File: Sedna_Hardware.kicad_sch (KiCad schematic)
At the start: 50 parts, among them J1 PJ-102A, J10 2-644803-3, J11 2-644488-3, J2 1935161, J3 1935161, J4 2-644488-2, J5 61201021721, J6 5-103634-2, J7 0878340619, J8 Conn_01x14, J9 2-644803-3, K1 ALDP105W, K2 ALDP105W, Q1 2N7000-D75Z, Q2 2N7000-D75Z, U1 LD1117V33, U2 ESP32-WROOM-32D-N16, U3 LM6511IMX/NOPB

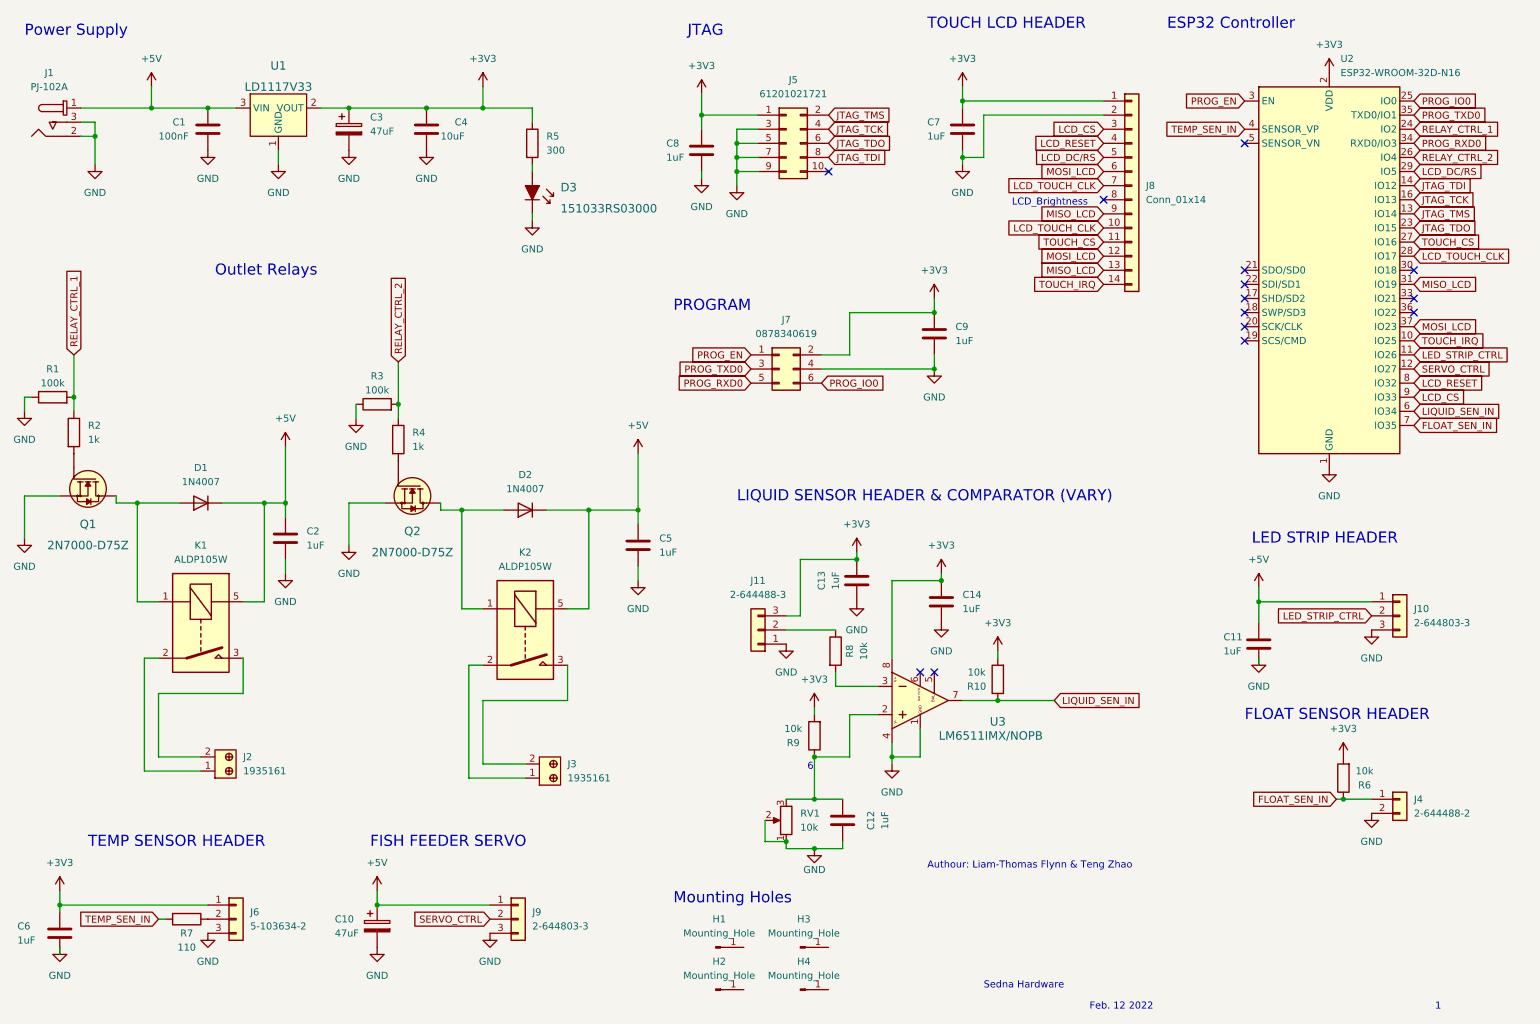
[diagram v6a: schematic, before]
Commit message: started layout tracks. Fixed regulator footprint
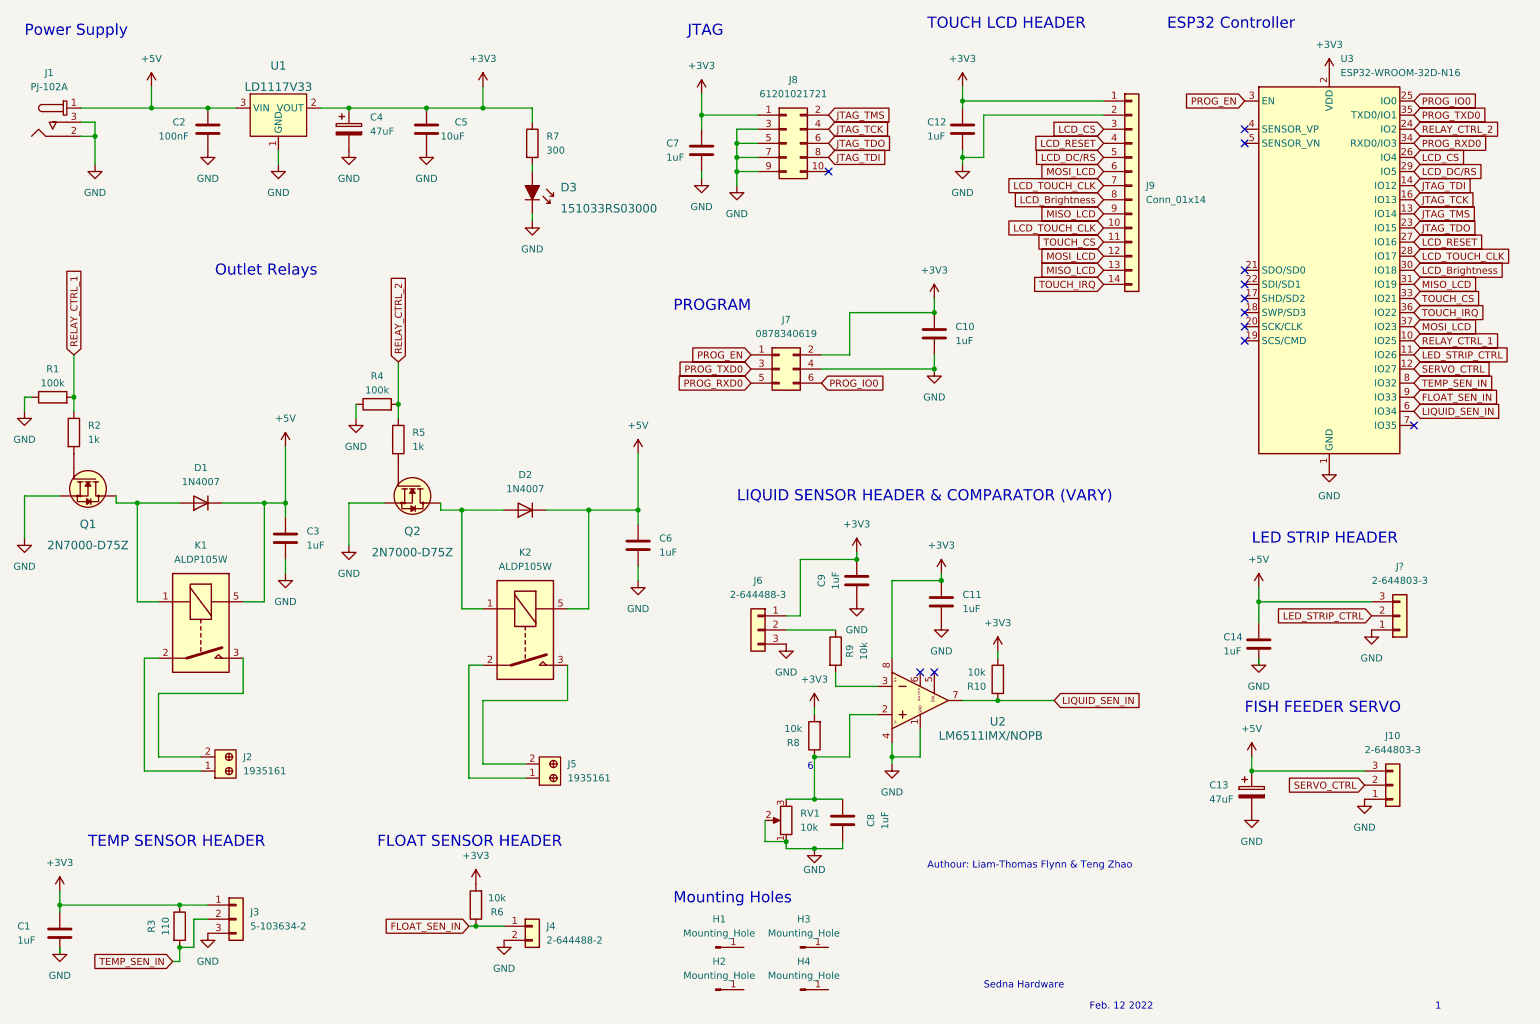
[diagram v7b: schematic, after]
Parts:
- removed J11: 2-644488-3, 2-644488-3:TE_2-644488-3, symbol Connector_Generic:Conn_01x03
- removed J9: 2-644803-3, 2-644803-3:TE_2-644803-3, symbol Connector_Generic:Conn_01x03
- removed R7: 110, Resistor_THT:R_Axial_DIN0204_L3.6mm_D1.6mm_P5.08mm_Horizontal, symbol Device:R
- added J6: 2-644488-3, 2-644488-3:TE_2-644488-3, symbol Connector_Generic:Conn_01x03
- added J?: 2-644803-3, 2-644803-3:TE_2-644803-3, symbol Connector_Generic:Conn_01x03
- added R3: 110, Resistor_THT:R_Axial_DIN0204_L3.6mm_D1.6mm_P5.08mm_Horizontal, symbol Device:R
- U1: footprint Package_TO_SOT_THT:TO-220-3_Horizontal_TabDown -> Package_TO_SOT_THT:TO-220-3_Horizontal_TabUp
- renumbered C6 to C1, C9 to C10, C14 to C11, C7 to C12, C10 to C13, C11 to C14, C1 to C2, C2 to C3, C3 to C4, C4 to C5, C5 to C6, C8 to C7, C12 to C8, C13 to C9, J6 to J3, J3 to J5, J5 to J8, J8 to J9, R3 to R4, R4 to R5, R5 to R7, R9 to R8, R8 to R9, U3 to U2, U2 to U3
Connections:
- net +3V3: now also J6.1 (Pin_1), R3.1
- net +5V: now also J10.3 (Pin_3), J?.3 (Pin_3); no longer J10.1 (Pin_1)
- net FLOAT_SEN_IN: now also U3.9 (IO33); no longer U3.7 (IO35)
- net GND: now also J10.1 (Pin_1), J6.3 (Pin_3), J?.1 (Pin_1); no longer J10.3 (Pin_3)
- net LCD_CS: now also U3.26 (IO4); no longer U3.9 (IO33)
- net LCD_RESET: now also U3.27 (IO16); no longer U3.8 (IO32)
- net LED_STRIP_CTRL: now also J?.2 (Pin_2); no longer J10.2 (Pin_2)
- net RELAY_CTRL_1: now also U3.10 (IO25); no longer U3.24 (IO2)
- net RELAY_CTRL_2: now also U3.24 (IO2); no longer U3.26 (IO4)
- net SERVO_CTRL: now also J10.2 (Pin_2)
- net TEMP_SEN_IN: now also J3.2 (Pin_2), U3.8 (IO32), R3.2; no longer U3.4 (SENSOR_VP)
- net TOUCH_CS: now also U3.33 (IO21); no longer U3.27 (IO16)
- net TOUCH_IRQ: now also U3.36 (IO22); no longer U3.10 (IO25)
- net LCD_Brightness: now reaches U3.30 (IO18)
- net LCD_Brightness: now also J9.8 (Pin_8)
- net at R9.1: now also J6.2 (Pin_2)
- no-connect marks 14 -> 12
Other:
- note removed: "LCD_Brightness"
- moved on the sheet: C13, J4, R6

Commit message: adjusted track size of power bus
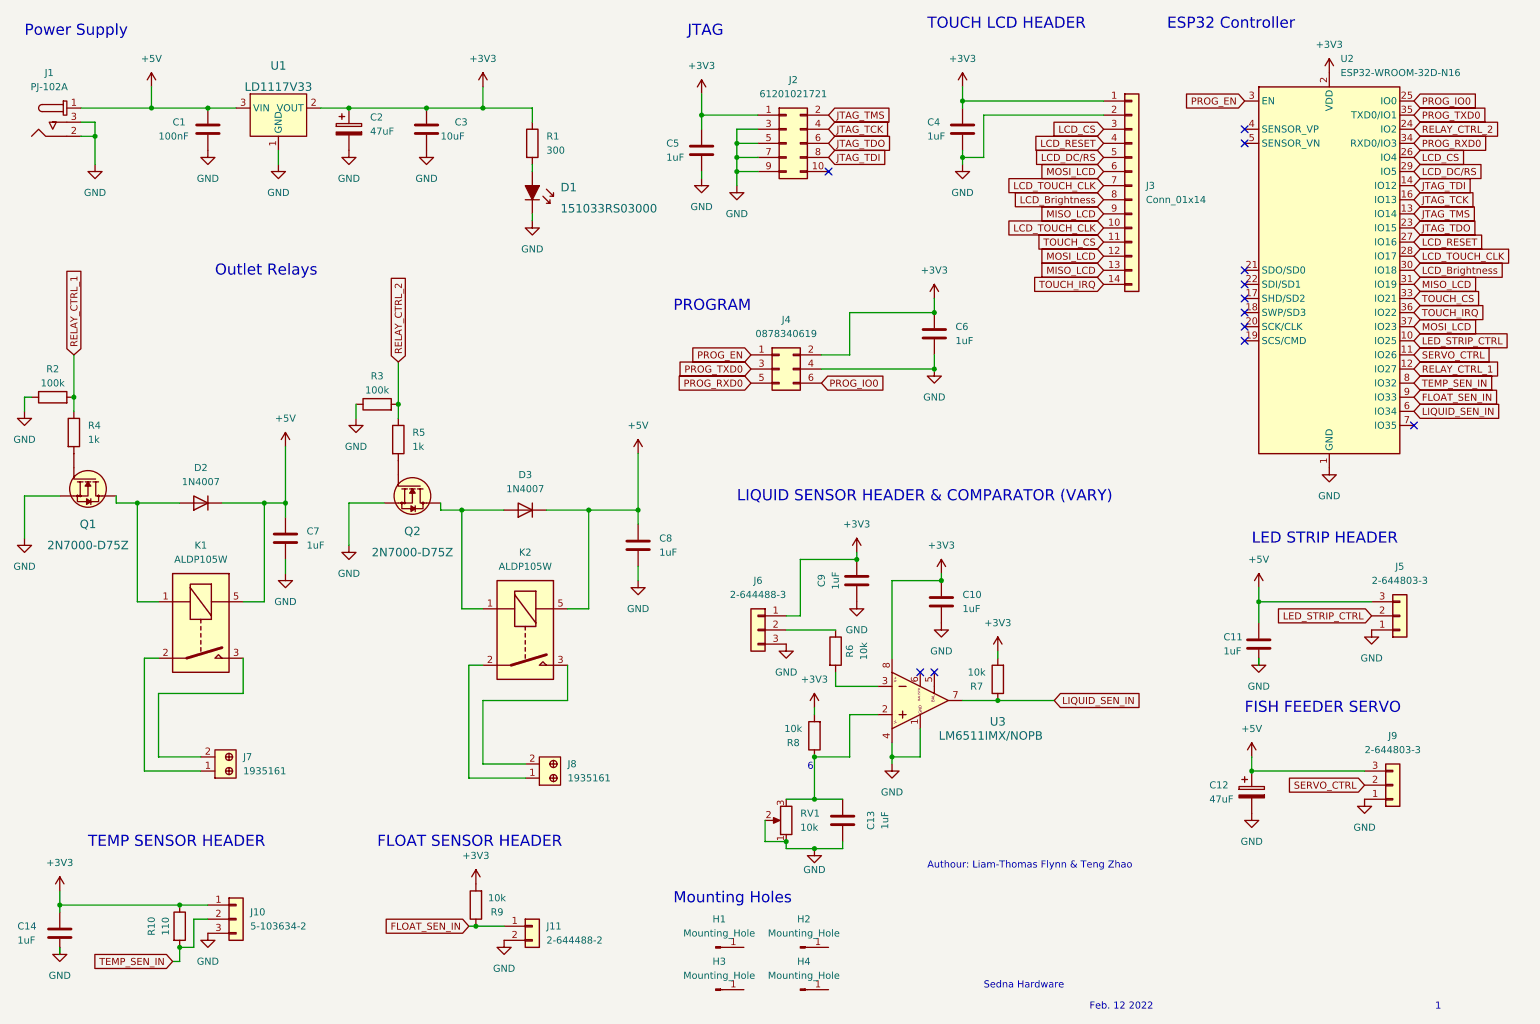
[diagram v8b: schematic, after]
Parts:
- gave numbers to parts that had none: 1
- renumbered C2 to C1, C11 to C10, C14 to C11, C13 to C12, C8 to C13, C1 to C14, C4 to C2, C5 to C3, C12 to C4, C7 to C5, C10 to C6, C3 to C7, C6 to C8, D3 to D1, D1 to D2, D2 to D3, H3 to H2, H2 to H3, J3 to J10, J4 to J11, J8 to J2, J9 to J3, J7 to J4, J2 to J7, J5 to J8, J10 to J9, R7 to R1, R3 to R10, R1 to R2, R4 to R3, R2 to R4, R9 to R6, R10 to R7, R6 to R9, U3 to U2, U2 to U3
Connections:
- net LED_STRIP_CTRL: now also U2.10 (IO25); no longer U2.11 (IO26)
- net RELAY_CTRL_1: now also U2.12 (IO27); no longer U2.10 (IO25)
- net SERVO_CTRL: now also U2.11 (IO26); no longer U2.12 (IO27)
